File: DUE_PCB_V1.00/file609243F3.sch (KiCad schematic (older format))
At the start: 27 parts, among them J26 Cutter1, J27 MotorR, J28 MotorL, J32 24V In, J37 RPM_Mow, J38 ODO_Left, J39 ODO_Right, J40 Motor_Right, J41 Motor_Left, J42 Cutter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

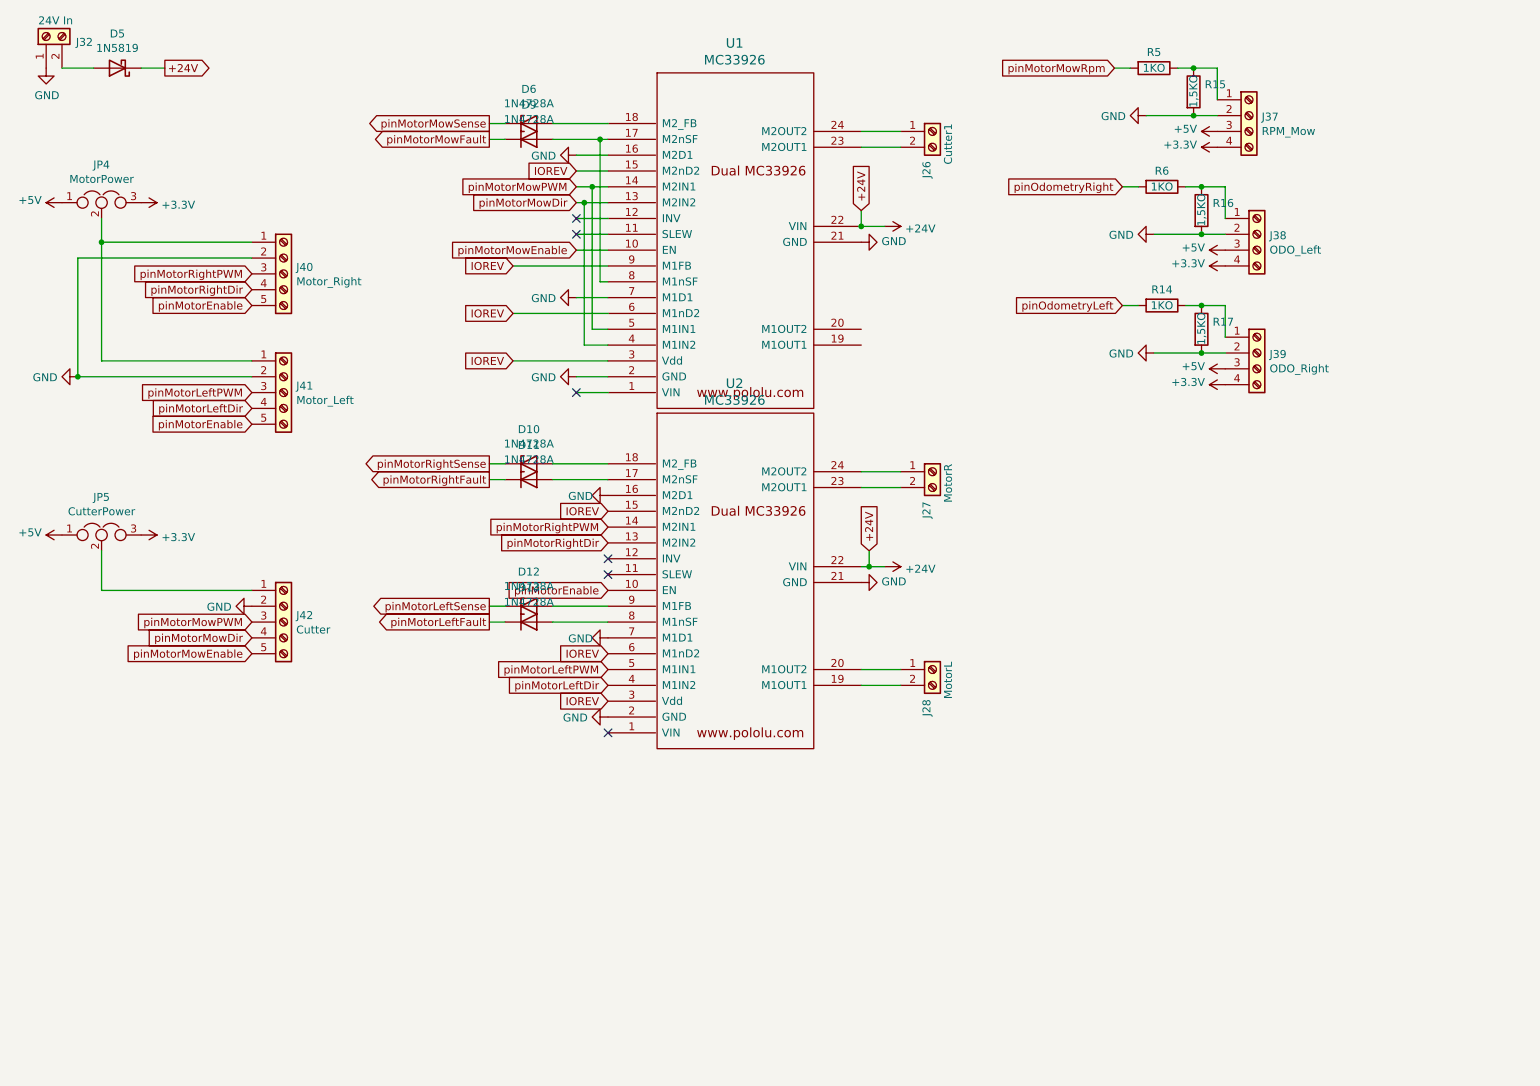
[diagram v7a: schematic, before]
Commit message: Remove 24V from PCB
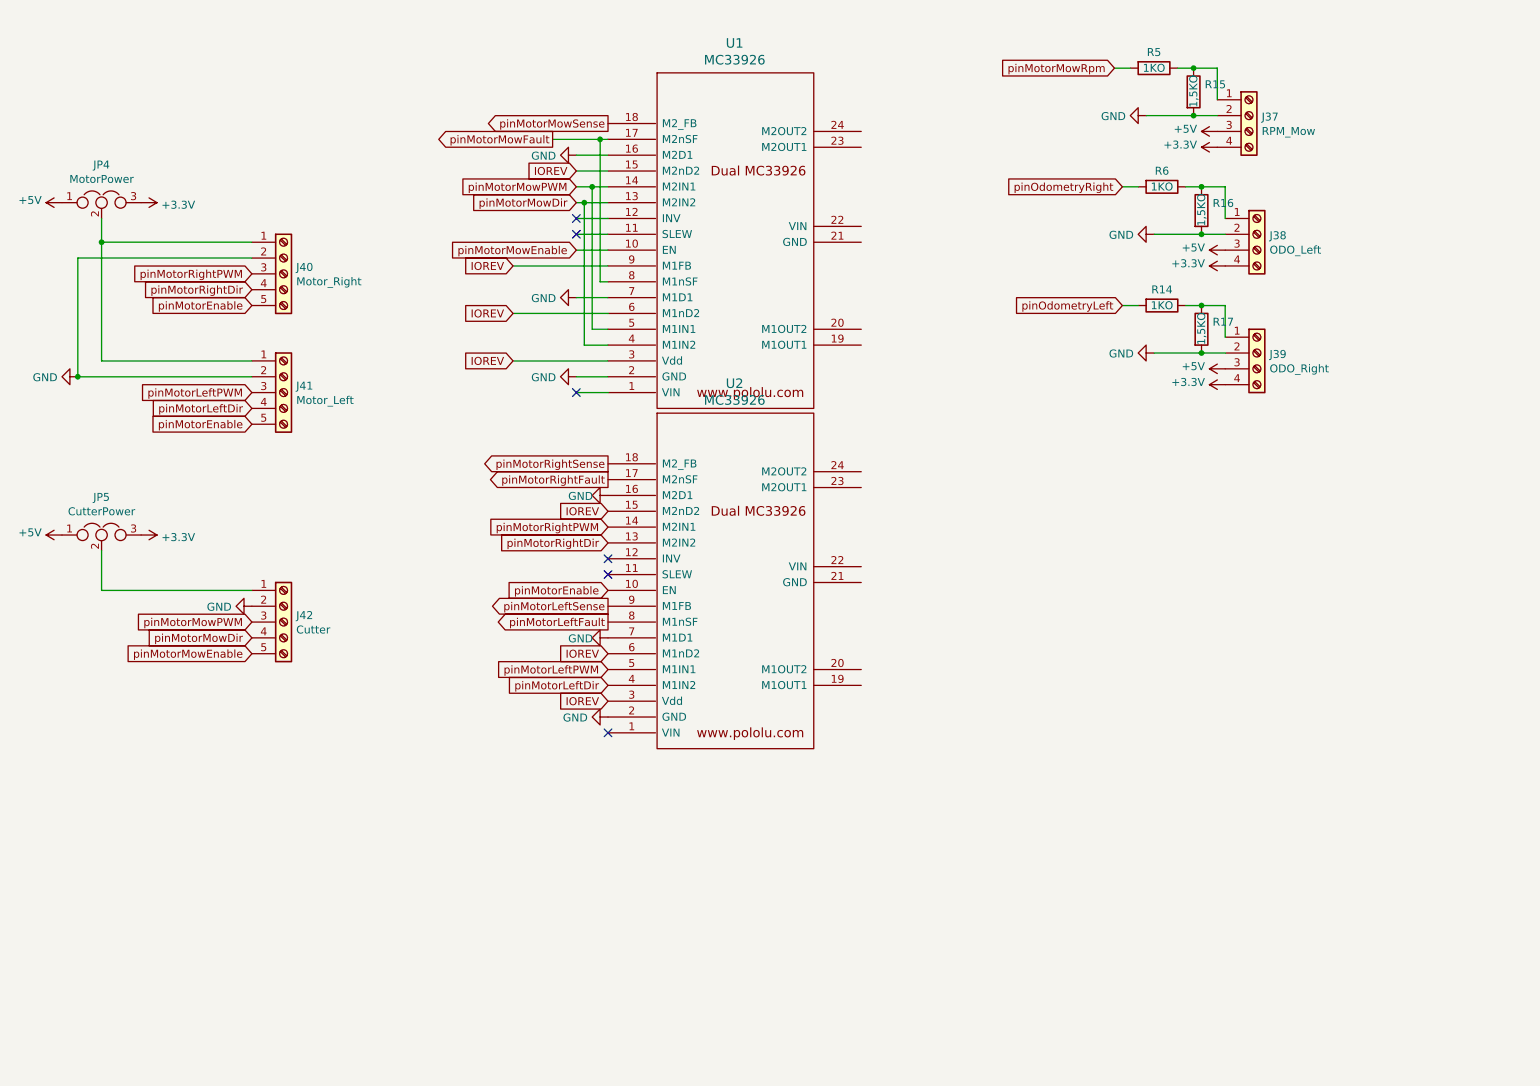
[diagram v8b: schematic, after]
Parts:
- removed D10, D11, D12, D13, D6, D9: 1N4728A, Diode_THT:D_DO-41_SOD81_P10.16mm_Horizontal, symbol Diode:1N47xxA
- removed D5: 1N5819, Diode_THT:D_DO-41_SOD81_P10.16mm_Horizontal, symbol Diode:1N5819
- removed J26: Cutter1, TerminalBlock:TerminalBlock_bornier-2_P5.08mm, symbol Connector:Screw_Terminal_01x02
- removed J27: MotorR, TerminalBlock:TerminalBlock_bornier-2_P5.08mm, symbol Connector:Screw_Terminal_01x02
- removed J28: MotorL, TerminalBlock:TerminalBlock_bornier-2_P5.08mm, symbol Connector:Screw_Terminal_01x02
- removed J32: 24V In, TerminalBlock:TerminalBlock_bornier-2_P5.08mm, symbol Connector:Screw_Terminal_01x02
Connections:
- net GND: no longer U1.21 (GND), U2.21 (GND)
- net pinMotorLeftFault: now also U2.8 (M1nSF)
- net pinMotorLeftSense: now also U2.9 (M1FB)
- net pinMotorMowFault: now also U1.17 (M2nSF), U1.8 (M1nSF)
- net pinMotorMowSense: now also U1.18 (M2_FB)
- net pinMotorRightFault: now also U2.17 (M2nSF)
- net pinMotorRightSense: now also U2.18 (M2_FB)
- net +24V: no longer names the net of U2.22 (VIN)
- net +24V: no longer U1.22 (VIN)
